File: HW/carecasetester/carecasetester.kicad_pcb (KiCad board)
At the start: 2 copper layers, 158.3 x 161.1 mm, 83 parts, among them J1 Conn_01x16_Female, J10-TP22 Conn_01x01_Male, J11-TP7 Conn_01x01_Male, J12-TP14 Conn_01x01_Male, J13-TP23 Conn_01x01_Male, J14-TP17 Conn_01x01_Male, J15 Conn_01x16_Male, J15-TP1 Conn_01x01_Male, J15-TP20 Conn_01x01_Male, J16-TP2 Conn_01x01_Male, J16-TP24 Conn_01x01_Male, J17-TP3 Conn_01x01_Male, J18-TP4 Conn_01x01_Male, J19-TP6 Conn_01x01_Male, J2 Conn_01x16_Female, J20-TP9 Conn_01x01_Male, J21-TP10 Conn_01x01_Male, J22-TP11 Conn_01x01_Male, J23-TP12 Conn_01x01_Male, J24-TP15 Conn_01x01_Male, J25-TP18 Conn_01x01_Male, J26-TP5 Conn_01x01_Male, J27-TP26 Conn_01x01_Male, J3 Conn_01x04_Female, J4 Conn_01x06_Male, J4-TP16 Conn_01x01_Male, J5 12V_Psu, J5-TP8 Conn_01x01_Male, J5-~E1 Conn_01x02_Male, J6-TP21 Conn_01x01_Male, J7-TP27 Conn_01x01_Male, J8-TP13 Conn_01x01_Male, J9-TP19 Conn_01x01_Male, K1 AZ952, K2 AZ952, Q1 BC847W, Q2 BC847W, SW1 SW_DIP_x02, U1 CD74HC4067M, U2 L7805

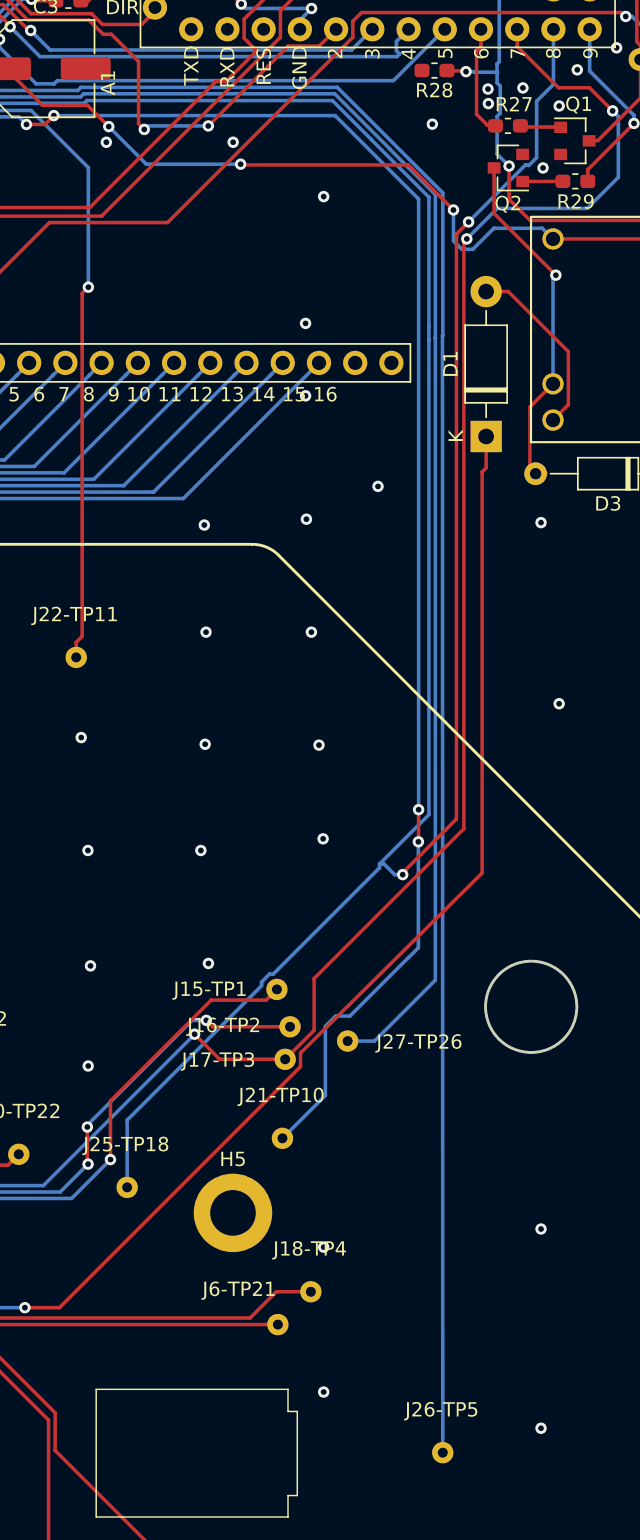
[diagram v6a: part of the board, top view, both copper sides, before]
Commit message: working speaker outputs set with pull down (internal arduino)
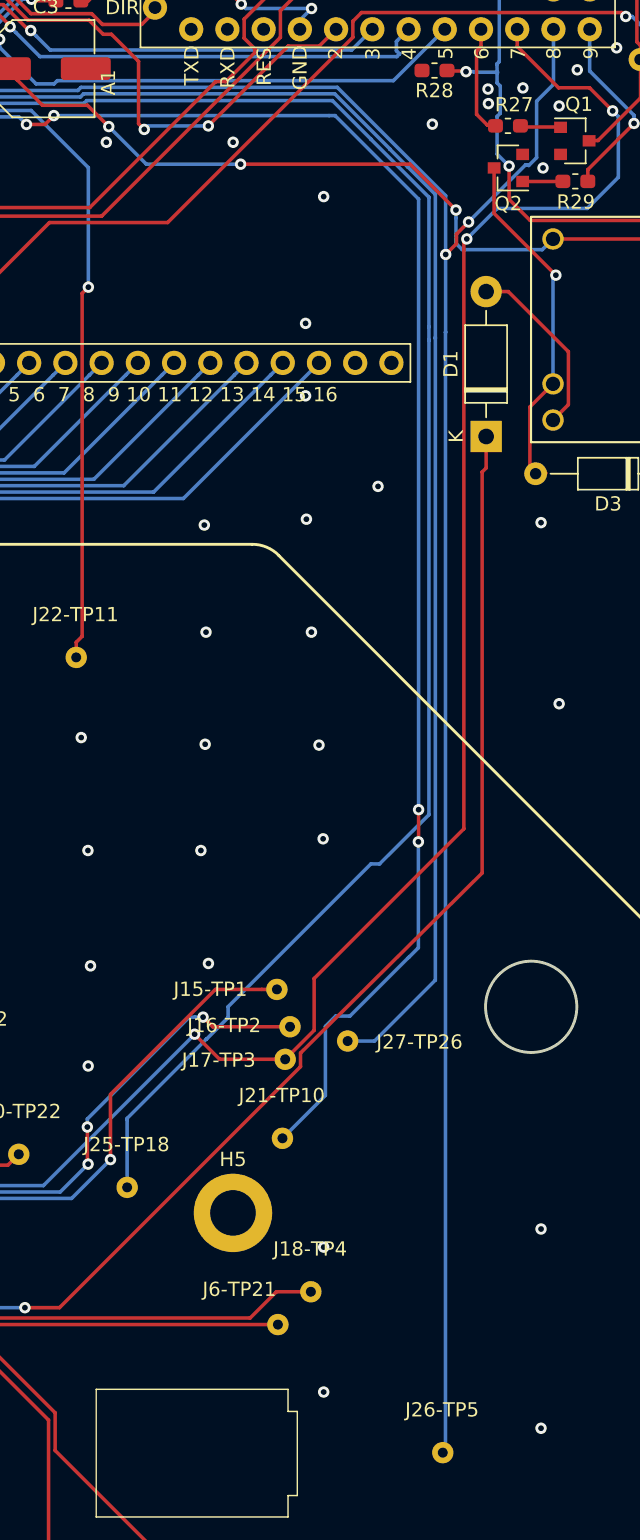
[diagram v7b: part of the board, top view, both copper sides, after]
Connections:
- J15 pad 12: /testpoints/TP5 -> Net-(J15-Pad12)
- J15 pad 13: Net-(J15-Pad13) -> /testpoints/TP5
- J25-TP18 pad 1: /testpoints/TP5 -> Net-(J15-Pad12)
- J26-TP5 pad 1: Net-(J15-Pad13) -> /testpoints/TP5
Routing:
- net Net-(J15-Pad13): track 185.0 -> 0.00 mm
- net Net-(J15-Pad12): track 0.00 -> 178.4 mm
- net /testpoints/TP5: track 243.9 -> 204.3 mm

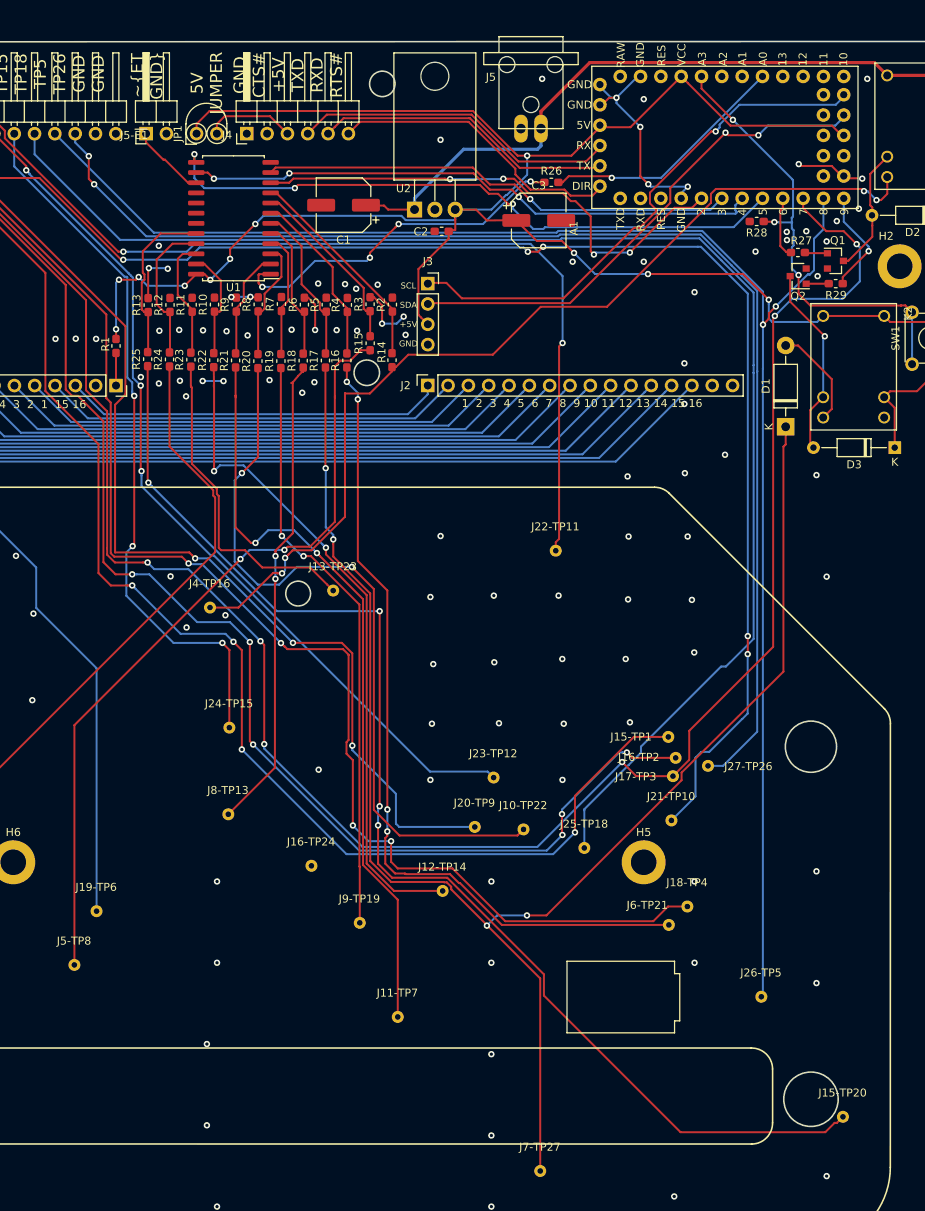
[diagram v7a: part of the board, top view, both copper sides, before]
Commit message: CC tester : tp25 added tp8 moved tp20 moved
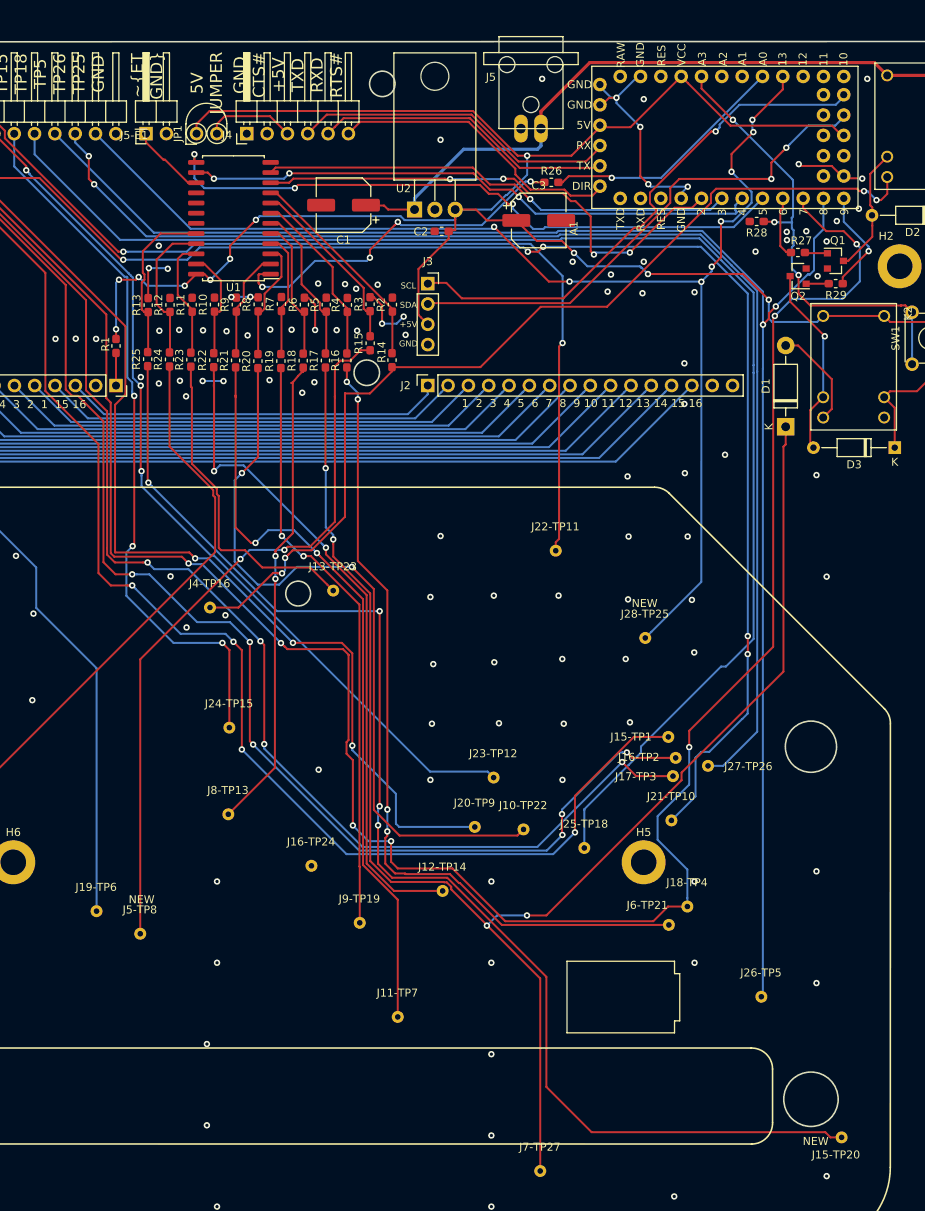
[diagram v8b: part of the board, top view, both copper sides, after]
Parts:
- added J28-TP25: Conn_01x01_Male, MM:P50-E-120-G(Pogo)_0.7mmHole_1.5mmPad, F.Cu at (194.5, 83.9)
- moved J5-TP8 9.11 mm to (131.4, 120.8)
- moved J15-TP20 2.58 mm to (219.0, 146.3)
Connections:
- A1 pad 24: (no net) -> /testpoints/TP25
- J15 pad 15: GND -> /testpoints/TP25
- J15 pad 4: /testpoints/TP4 -> Net-(J15-Pad4)
- J15 pad 5: Net-(J15-Pad5) -> /testpoints/TP4
- J17-TP3 pad 1: /testpoints/TP4 -> Net-(J15-Pad4)
- J18-TP4 pad 1: Net-(J15-Pad5) -> /testpoints/TP4
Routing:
- net Net-(J15-Pad5): track 172.0 -> 0.00 mm, vias 4 -> 0
- net Net-(J15-Pad4): track 0.00 -> 166.9 mm, vias 0 -> 4
- net /testpoints/TP25: track 0.00 -> 164.0 mm, vias 0 -> 8
- net /testpoints/TP4: track 256.6 -> 280.3 mm, vias 6 -> 7
- net Net-(J5-TP8-Pad1): track 98.0 -> 90.7 mm
- net Net-(J15-TP20-Pad1): track 156.2 -> 162.0 mm
- net /display/SDA: track 63.0 -> 63.9 mm
- net Net-(R26-Pad1): track 44.4 -> 44.9 mm
- net GND: vias 157 -> 160
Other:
- board text added: "DCTMM_CC-TESTER V0.22 03/08/2020"
- board text added: "GND TP1 TP2 TP3 TP4 TP6 TP9 TP10 TP11 TP12 TP15 TP18 TP5 TP26 TP25 GND"
- board text added: "NEW"
- board text removed: "DCTMM_CC-TESTER V0.21 06/04/2020"
